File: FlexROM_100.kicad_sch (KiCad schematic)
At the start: 6 parts

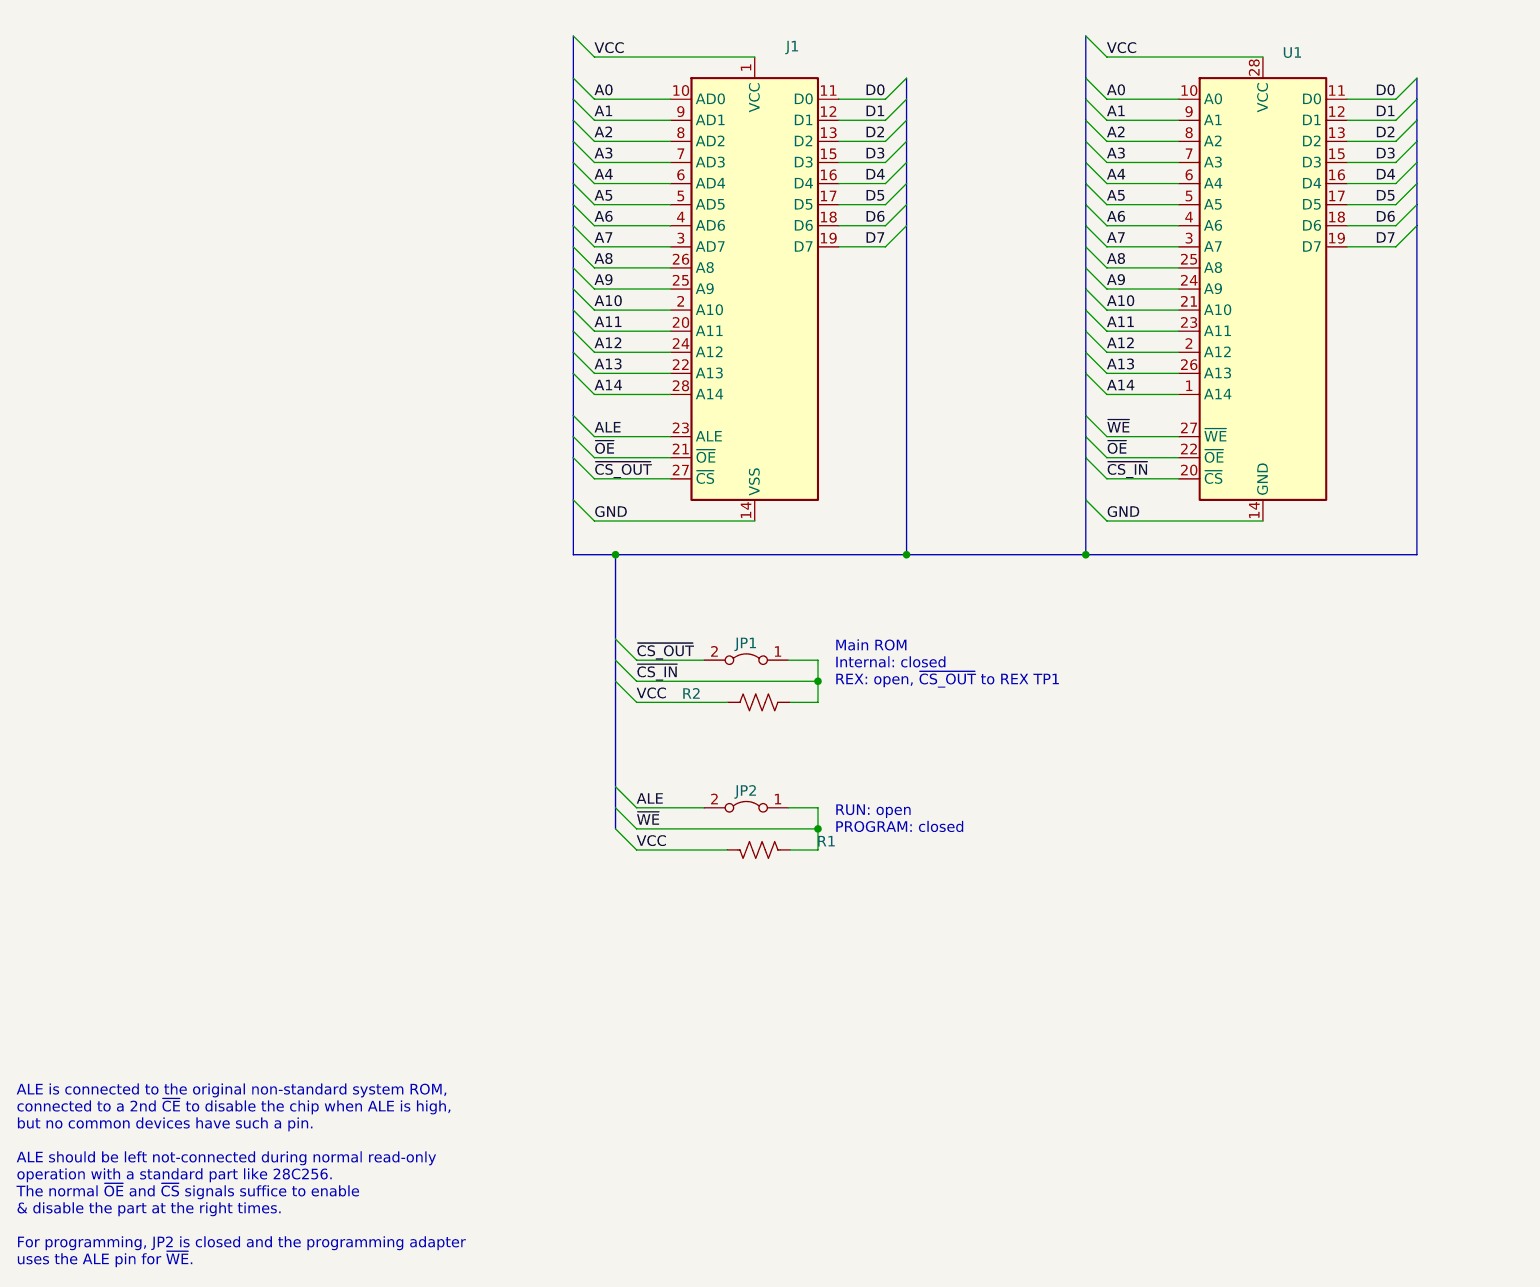
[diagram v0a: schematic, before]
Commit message: programming adapter board outline & ground pour
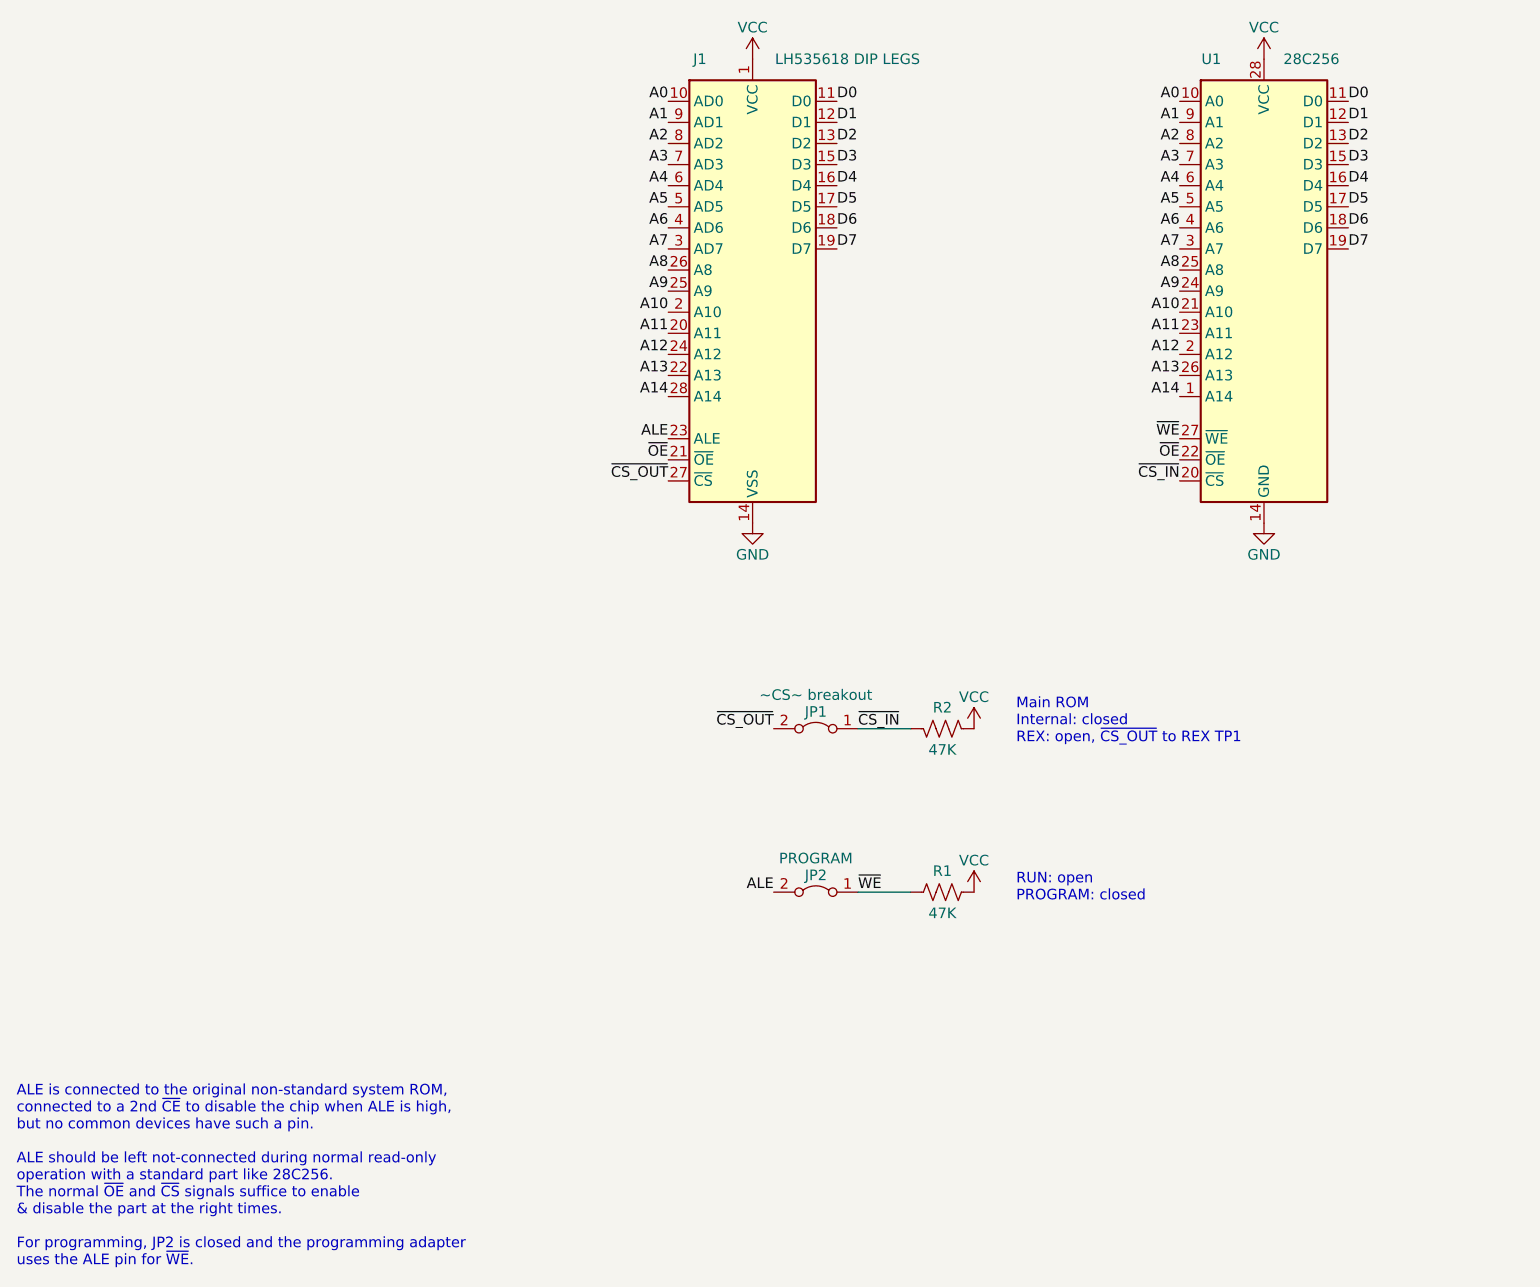
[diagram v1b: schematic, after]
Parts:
- J1: value (none) -> LH535618 DIP LEGS; footprint (none) -> 000_LOCAL:DIP28_0.6_pcb
- JP1: value (none) -> ~CS~ breakout; footprint (none) -> 000_LOCAL:Pin_Header_Angled_1x02_Pitch2.54mm
- JP2: value (none) -> PROGRAM; footprint (none) -> 000_LOCAL:Pin_Header_Angled_1x02_Pitch2.54mm
- R1, R2: value (none) -> 47K; footprint (none) -> 000_LOCAL:R_0805
- U1: value (none) -> 28C256; footprint (none) -> 000_LOCAL:SOIC28W
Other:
- moved on the sheet: JP1, JP2, R1, R2

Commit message: various minor cleanups
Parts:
- JP1: value ~CS~ breakout -> ~{CS} breakout
- JP2: value PROGRAM -> PROGRAM/RUN
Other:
- note added: "Main ROM Internal: close REX: open, connect ~{CS_OUT} to REX TP1"
- note added: "RUN: open PROGRAM: close"
- note removed: "Main ROM Internal: closed REX: open, ~{CS_OUT} to REX TP1"
- note removed: "RUN: open PROGRAM: closed"
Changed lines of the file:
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@@
     (stroke (width 0) (type default) (color 0 0 0 0))
   )
-  (text "RUN: open\nPROGRAM: closed" (at 139.7 151.13 0)
-    (effects (font (size 1.27 1.27)) (justify left bottom))
-  )
-  (text "Main ROM\nInternal: closed\nREX: open, ~{CS_OUT} to REX TP1\n"
+  (text "RUN: open\nPROGRAM: close" (at 139.7 151.13 0)
+    (effects (font (size 1.27 1.27)) (justify left bottom))
+  )
+  (text "Main ROM\nInternal: close\nREX: open, connect ~{CS_OUT} to REX TP1\n"
     (at 139.7 132.08 0)
     (effects (font (size 1.27 1.27)) (justify left bottom))
@@
     (in_bom yes) (on_board yes)
     (property "Reference" "JP1" (id 0) (at 115.57 128.143 0))
-    (property "Value" "~CS~ breakout" (id 1) (at 115.57 126.111 0))
+    (property "Value" "~{CS} breakout" (id 1) (at 115.57 126.111 0))
     (property "Footprint" "000_LOCAL:Pin_Header_Angled_1x02_Pitch2.54mm" (id 2) (at 115.57 130.175 0)
       (effects (font (size 1.27 1.27)) hide)
@@
     (in_bom yes) (on_board yes)
     (property "Reference" "JP2" (id 0) (at 115.57 147.828 0))
-    (property "Value" "PROGRAM" (id 1) (at 115.57 145.796 0))
+    (property "Value" "PROGRAM/RUN" (id 1) (at 115.57 145.796 0))
     (property "Footprint" "000_LOCAL:Pin_Header_Angled_1x02_Pitch2.54mm" (id 2) (at 115.57 149.86 0)
       (effects (font (size 1.27 1.27)) hide)
@@
     )
     (path "/00000000-0000-0000-0000-00005e68b8a2"
-      (reference "JP1") (unit 1) (value "~CS~ breakout") (footprint "000_LOCAL:Pin_Header_Angled_1x02_Pitch2.54mm")
+      (reference "JP1") (unit 1) (value "~{CS} breakout") (footprint "000_LOCAL:Pin_Header_Angled_1x02_Pitch2.54mm")
     )
     (path "/00000000-0000-0000-0000-00005fbfb30e"
-      (reference "JP2") (unit 1) (value "PROGRAM") (footprint "000_LOCAL:Pin_Header_Angled_1x02_Pitch2.54mm")
+      (reference "JP2") (unit 1) (value "PROGRAM/RUN") (footprint "000_LOCAL:Pin_Header_Angled_1x02_Pitch2.54mm")
     )
     (path "/00000000-0000-0000-0000-00005fbfb319"

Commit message: minor touches
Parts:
- R1, R2: value 47K -> 100K
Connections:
- net ~{CS_IN} renamed ~{CS_IC}
- net ~{CS_OUT} renamed ~{CS_BUS}
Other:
- note added: "JP1 - Main ROM Source Boot from internal: close Boot from REX: open, connect ~{CS_BUS} to REX TP1"
- note added: "Pin 23 ALE is a 2nd ~{CE} on the original non-standard pinout system ROM. (disable the chip when ALE is high) ALE should be left not-connected during normal read-only operation with a standard part like 28C256. The normal ~{OE} and ~{CS} signals suffice to enable & disable the part at the right times. For programming, JP2 is closed and the programming adapter routes the ALE pin to ~{WE}."
- note removed: "ALE is connected to the original non-standard system ROM, connected to a 2nd ~{CE} to disable the chip when ALE is high, but no common devices have such a pin. ALE should be left not-connected during normal read-only operation with a standard part like 28C256. The normal ~{OE} and ~{CS} signals suffice to enable & disable the part at the right times. For programming, JP2 is closed and the program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"
- note removed: "Main ROM Internal: close REX: open, connect ~{CS_OUT} to REX TP1"
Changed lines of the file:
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@@
   (title_block
     (title "28C256 SOIC to LH535618 DIP")
-    (date "2022-10-12")
-    (rev "003")
+    (date "2023-02-23")
+    (rev "004")
     (company "Brian K. White - b.kenyon.w@gmail.com")
     (comment 1 "TRS-80 Model 100 system rom M12")
@@
     (effects (font (size 1.27 1.27)) (justify left bottom))
   )
-  (text "Main ROM\nInternal: close\nREX: open, connect ~{CS_OUT} to REX TP1\n"
+  (text "JP1 - Main ROM Source\nBoot from internal: close\nBoot from REX: open, connect ~{CS_BUS} to REX TP1\n"
     (at 139.7 132.08 0)
     (effects (font (size 1.27 1.27)) (justify left bottom))
   )
-  (text "ALE is connected to the original non-standard system ROM,\nconnected to a 2nd ~{CE} to disable the chip when ALE is high,\nbut no common devices have such a pin.\n\nALE should be left not-connected during normal read-only\noperation with a standard part like 28C256.\nThe normal ~{OE} and ~{CS} signals suffice to enable\n& disable the part at the right times.\n\nFor programming, JP2 is closed and the programming adapter\nuses the ALE pin for ~{WE}."
+  (text "Pin 23 ALE is a 2nd ~{CE} on the original non-standard pinout system ROM.\n(disable the chip when ALE is high)\n\nALE should be left not-connected during normal read-only operation with a standard part like 28C256.\nThe normal ~{OE} and ~{CS} signals suffice to enable & disable the part at the right times.\n\nFor programming, JP2 is closed and the programming adapter routes the ALE pin to ~{WE}."
     (at 19.304 195.072 0)
     (effects (font (size 1.27 1.27)) (justify left bottom))
@@
     (effects (font (size 1.27 1.27)) (justify left bottom))
   )
-  (label "~{CS_OUT}" (at 110.49 130.175 180)
+  (label "~{CS_BUS}" (at 110.49 130.175 180)
     (effects (font (size 1.27 1.27)) (justify right bottom))
   )
@@
     (effects (font (size 1.27 1.27)) (justify left bottom))
   )
-  (label "~{CS_IN}" (at 159.385 100.33 180)
+  (label "~{CS_IC}" (at 159.385 100.33 180)
     (effects (font (size 1.27 1.27)) (justify right bottom))
   )
@@
     (effects (font (size 1.27 1.27)) (justify left bottom))
   )
-  (label "~{CS_IN}" (at 120.65 130.175 0)
+  (label "~{CS_IC}" (at 120.65 130.175 0)
     (effects (font (size 1.27 1.27)) (justify left bottom))
   )
@@
     (effects (font (size 1.27 1.27)) (justify right bottom))
   )
-  (label "~{CS_OUT}" (at 97.79 100.33 180)
+  (label "~{CS_BUS}" (at 97.79 100.33 180)
     (effects (font (size 1.27 1.27)) (justify right bottom))
   )
@@
     (in_bom yes) (on_board yes)
     (property "Reference" "R2" (id 0) (at 130.81 127.635 90))
-    (property "Value" "47K" (id 1) (at 130.81 132.715 90))
+    (property "Value" "100K" (id 1) (at 130.81 132.715 90))
     (property "Footprint" "000_LOCAL:R_0805" (id 2) (at 130.81 130.175 0)
       (effects (font (size 1.27 1.27)) hide)
@@
     (in_bom yes) (on_board yes)
     (property "Reference" "R1" (id 0) (at 130.81 147.32 90))
-    (property "Value" "47K" (id 1) (at 130.81 152.4 90))
+    (property "Value" "100K" (id 1) (at 130.81 152.4 90))
     (property "Footprint" "000_LOCAL:R_0805" (id 2) (at 130.81 149.86 0)
       (effects (font (size 1.27 1.27)) hide)
@@
     )
     (path "/00000000-0000-0000-0000-00005fbfb319"
-      (reference "R1") (unit 1) (value "47K") (footprint "000_LOCAL:R_0805")
+      (reference "R1") (unit 1) (value "100K") (footprint "000_LOCAL:R_0805")
     )
     (path "/00000000-0000-0000-0000-00005e68c7f8"
-      (reference "R2") (unit 1) (value "47K") (footprint "000_LOCAL:R_0805")
+      (reference "R2") (unit 1) (value "100K") (footprint "000_LOCAL:R_0805")
     )
     (path "/00000000-0000-0000-0000-00005e5b130a"
